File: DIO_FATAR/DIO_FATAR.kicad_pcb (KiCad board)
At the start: 2 copper layers, 92 x 57 mm, 22 parts, among them J1 in, J2 thru, J3 right, J4 left, U1 74HC595, U2 74HC595, U3 74165, U4 74165

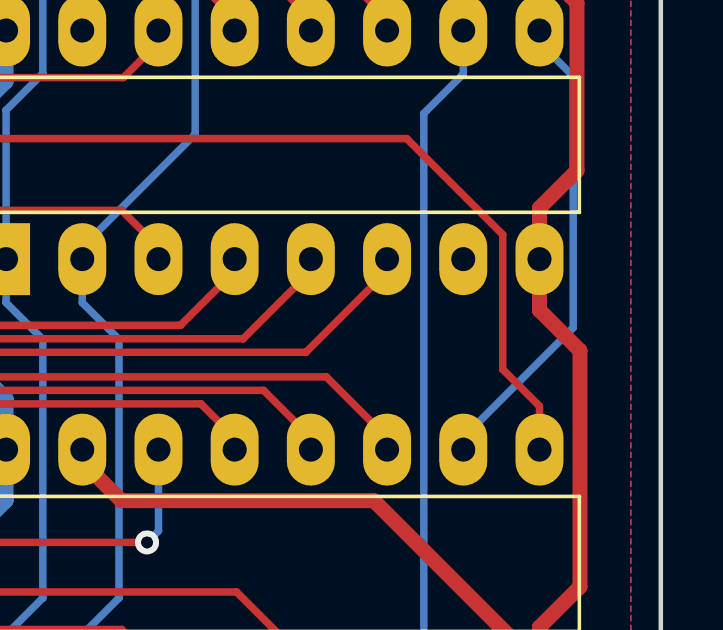
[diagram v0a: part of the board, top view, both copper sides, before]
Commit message: DIO_FATAR: add vias to fill a small empty space
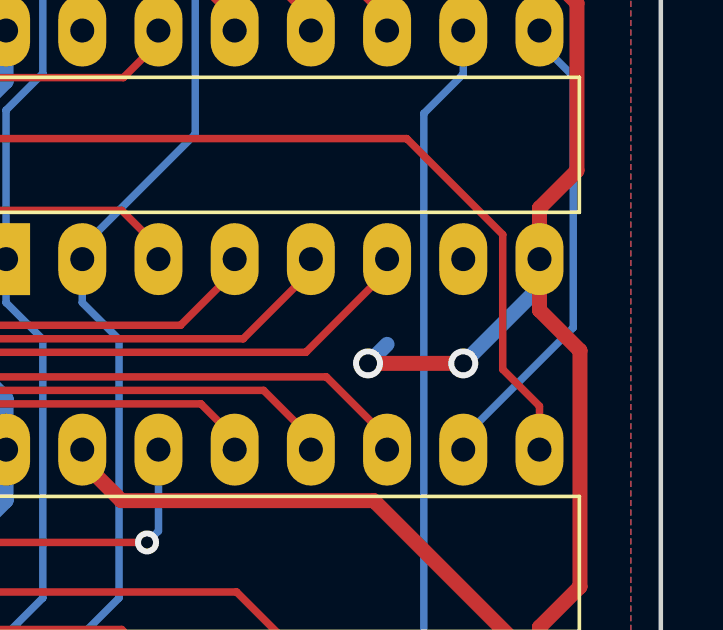
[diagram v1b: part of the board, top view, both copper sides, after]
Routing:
- net GND: track 320.9 -> 329.5 mm, vias 4 -> 6
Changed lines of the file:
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@@
     (thickness 1.6)
     (drawings 4)
-    (tracks 536)
+    (tracks 542)
     (zones 0)
     (modules 22)
@@
   (segment (start 139.458001 56.749999) (end 134.045001 56.749999) (width 0.5) (layer F.Cu) (net 1))
   (segment (start 140.208 56) (end 139.458001 56.749999) (width 0.5) (layer F.Cu) (net 1))
-  (segment (start 130.81 86.06) (end 130.81 85.66) (width 0.25) (layer F.Cu) (net 7))
-  (segment (start 130.81 72.09) (end 130.81 72.49) (width 0.25) (layer B.Cu) (net 7))
-  (segment (start 130.81 71.69) (end 130.81 72.09) (width 0.25) (layer B.Cu) (net 7))
-  (segment (start 140.97 72.49) (end 140.97 72.09) (width 0.25) (layer F.Cu) (net 17))
-  (segment (start 138.43 72.49) (end 138.43 72.09) (width 0.25) (layer F.Cu) (net 19))
-  (segment (start 135.89 72.49) (end 135.89 72.09) (width 0.25) (layer F.Cu) (net 21))
-  (segment (start 133.35 72.09) (end 133.35 71.69) (width 0.25) (layer F.Cu) (net 5))
-  (segment (start 118.745 76.2) (end 114.935 76.2) (width 0.25) (layer F.Cu) (net 21))
-  (segment (start 120.65 74.295) (end 118.745 76.2) (width 0.25) (layer F.Cu) (net 21))
-  (segment (start 135.89 64.47) (end 135.89 64.87) (width 0.25) (layer F.Cu) (net 23))
-  (segment (start 138.43 64.47) (end 138.43 64.07) (width 0.25) (layer F.Cu) (net 25))
-  (segment (start 140.97 64.47) (end 140.97 64.07) (width 0.25) (layer F.Cu) (net 27))
-  (segment (start 140.97 78.44) (end 140.97 78.04) (width 0.25) (layer F.Cu) (net 32))
-  (segment (start 138.43 78.44) (end 138.43 78.04) (width 0.25) (layer F.Cu) (net 33))
   (segment (start 133.35 78.44) (end 133.35 78.84) (width 0.25) (layer B.Cu) (net 2))
   (via (at 134.62 60.452) (size 1) (drill 0.6) (layers F.Cu B.Cu) (net 2))
@@
   (segment (start 130.81 57.865002) (end 133.396998 60.452) (width 0.5) (layer F.Cu) (net 2))
   (segment (start 130.81 54.164998) (end 130.81 57.865002) (width 0.5) (layer F.Cu) (net 2))
+  (segment (start 147.955 72.09) (end 147.955 73.025) (width 0.5) (layer B.Cu) (net 2))
+  (via (at 145.415 75.565) (size 1) (drill 0.6) (layers F.Cu B.Cu) (net 2))
+  (segment (start 147.955 73.025) (end 145.415 75.565) (width 0.5) (layer B.Cu) (net 2))
+  (via (at 142.24 75.565) (size 1) (drill 0.6) (layers F.Cu B.Cu) (net 2))
+  (segment (start 145.415 75.565) (end 142.24 75.565) (width 0.5) (layer F.Cu) (net 2))
+  (segment (start 142.24 75.565) (end 142.875 74.93) (width 0.5) (layer B.Cu) (net 2))
   (via (at 109.22 63.246) (size 0.8) (drill 0.4) (layers F.Cu B.Cu) (net 3))
   (segment (start 107.95 56.515) (end 107.95 61.976) (width 0.25) (layer F.Cu) (net 3))
@@
   (segment (start 105.537 51.562) (end 107.95 53.975) (width 0.25) (layer B.Cu) (net 4))
   (segment (start 91.694 51.562) (end 105.537 51.562) (width 0.25) (layer B.Cu) (net 4))
+  (segment (start 133.35 72.09) (end 133.35 71.69) (width 0.25) (layer F.Cu) (net 5))
   (segment (start 110.49 56.515) (end 110.49 53.975) (width 0.25) (layer B.Cu) (net 5))
   (segment (start 132.715 84.61) (end 132.715 86.06) (width 0.25) (layer B.Cu) (net 5))
@@
   (segment (start 136.48001 67.92499) (end 132.715 71.69) (width 0.25) (layer B.Cu) (net 5))
   (segment (start 110.49 53.975) (end 111.778601 52.686399) (width 0.25) (layer B.Cu) (net 5))
+  (segment (start 130.81 86.06) (end 130.81 85.66) (width 0.25) (layer F.Cu) (net 7))
+  (segment (start 130.81 72.09) (end 130.81 72.49) (width 0.25) (layer B.Cu) (net 7))
+  (segment (start 130.81 71.69) (end 130.81 72.09) (width 0.25) (layer B.Cu) (net 7))
   (segment (start 130.175 84.61) (end 130.175 86.06) (width 0.25) (layer B.Cu) (net 7))
   (segment (start 131.40001 83.38499) (end 130.175 84.61) (width 0.25) (layer B.Cu) (net 7))
@@
   (segment (start 95.866001 68.180001) (end 81.750001 68.180001) (width 0.25) (layer B.Cu) (net 16))
   (segment (start 96.266 68.58) (end 95.866001 68.180001) (width 0.25) (layer B.Cu) (net 16))
+  (segment (start 140.97 72.49) (end 140.97 72.09) (width 0.25) (layer F.Cu) (net 17))
   (segment (start 138.07999 74.74501) (end 140.335 72.49) (width 0.25) (layer F.Cu) (net 17))
   (segment (start 125.27999 74.74501) (end 138.07999 74.74501) (width 0.25) (layer F.Cu) (net 17))
@@
   (segment (start 94.488 76.708) (end 99.06 81.28) (width 0.25) (layer B.Cu) (net 18))
   (segment (start 80.118 76.708) (end 94.488 76.708) (width 0.25) (layer B.Cu) (net 18))
+  (segment (start 138.43 72.49) (end 138.43 72.09) (width 0.25) (layer F.Cu) (net 19))
   (segment (start 137.795 72.49) (end 137.795 72.09) (width 0.25) (layer F.Cu) (net 19))
   (segment (start 135.99 74.295) (end 137.795 72.49) (width 0.25) (layer F.Cu) (net 19))
@@
   (segment (start 96.012 75.692) (end 99.06 78.74) (width 0.25) (layer B.Cu) (net 20))
   (segment (start 81.642 75.692) (end 96.012 75.692) (width 0.25) (layer B.Cu) (net 20))
+  (segment (start 135.89 72.49) (end 135.89 72.09) (width 0.25) (layer F.Cu) (net 21))
+  (segment (start 118.745 76.2) (end 114.935 76.2) (width 0.25) (layer F.Cu) (net 21))
+  (segment (start 120.65 74.295) (end 118.745 76.2) (width 0.25) (layer F.Cu) (net 21))
   (segment (start 135.255 71.69) (end 135.255 72.09) (width 0.25) (layer F.Cu) (net 21))
   (segment (start 134.02999 70.46499) (end 135.255 71.69) (width 0.25) (layer F.Cu) (net 21))
@@
   (segment (start 97.536 74.676) (end 99.06 76.2) (width 0.25) (layer B.Cu) (net 22))
   (segment (start 83.166 74.676) (end 97.536 74.676) (width 0.25) (layer B.Cu) (net 22))
+  (segment (start 135.89 64.47) (end 135.89 64.87) (width 0.25) (layer F.Cu) (net 23))
   (segment (start 119.850001 71.919999) (end 120.65 71.12) (width 0.25) (layer F.Cu) (net 23))
   (segment (start 118.973599 72.796401) (end 119.850001 71.919999) (width 0.25) (layer F.Cu) (net 23))
@@
   (segment (start 82.55 71.52) (end 84.69 73.66) (width 0.25) (layer B.Cu) (net 24))
   (segment (start 82.55 71.12) (end 82.55 71.52) (width 0.25) (layer B.Cu) (net 24))
+  (segment (start 138.43 64.47) (end 138.43 64.07) (width 0.25) (layer F.Cu) (net 25))
   (segment (start 137.795 64.07) (end 137.795 64.47) (width 0.25) (layer F.Cu) (net 25))
   (segment (start 136.66999 62.94499) (end 137.795 64.07) (width 0.25) (layer F.Cu) (net 25))
@@
   (segment (start 85.09 71.52) (end 86.21501 72.64501) (width 0.25) (layer B.Cu) (net 26))
   (segment (start 85.09 71.12) (end 85.09 71.52) (width 0.25) (layer B.Cu) (net 26))
+  (segment (start 140.97 64.47) (end 140.97 64.07) (width 0.25) (layer F.Cu) (net 27))
   (segment (start 118.11 68.58) (end 120.65 66.04) (width 0.25) (layer F.Cu) (net 27))
   (segment (start 114.935 68.58) (end 118.11 68.58) (width 0.25) (layer F.Cu) (net 27))
@@
   (segment (start 102.235 66.675) (end 101.6 66.04) (width 0.25) (layer B.Cu) (net 31))
   (segment (start 106.68 66.675) (end 102.235 66.675) (width 0.25) (layer B.Cu) (net 31))
+  (segment (start 140.97 78.44) (end 140.97 78.04) (width 0.25) (layer F.Cu) (net 32))
   (segment (start 102.235 69.215) (end 101.6 68.58) (width 0.25) (layer B.Cu) (net 32))
   (segment (start 106.68 69.215) (end 102.235 69.215) (width 0.25) (layer B.Cu) (net 32))
@@
   (segment (start 122.555 72.39) (end 122.555 71.359998) (width 0.25) (layer B.Cu) (net 32))
   (segment (start 127.635 77.47) (end 122.555 72.39) (width 0.25) (layer B.Cu) (net 32))
+  (segment (start 138.43 78.44) (end 138.43 78.04) (width 0.25) (layer F.Cu) (net 33))
   (segment (start 102.235 71.755) (end 101.6 71.12) (width 0.25) (layer B.Cu) (net 33))
   (segment (start 106.68 71.755) (end 102.235 71.755) (width 0.25) (layer B.Cu) (net 33))
@@
   (segment (start 125.73 85.725) (end 124.46 85.725) (width 0.25) (layer F.Cu) (net 38))
   (segment (start 128.14001 88.13501) (end 125.73 85.725) (width 0.25) (layer F.Cu) (net 38))
-  (segment (start 149.08001 74.37499) (end 145.415 78.04) (width 0.25) (layer B.Cu) (net 52))
-  (segment (start 145.415 78.04) (end 145.415 78.44) (width 0.25) (layer B.Cu) (net 52))
-  (segment (start 149.08001 65.99501) (end 149.08001 74.37499) (width 0.25) (layer B.Cu) (net 52))
-  (segment (start 147.955 64.87) (end 149.08001 65.99501) (width 0.25) (layer B.Cu) (net 52))
-  (segment (start 147.955 64.47) (end 147.955 64.87) (width 0.25) (layer B.Cu) (net 52))
   (segment (start 83.82 74.53) (end 83.82 67.31) (width 0.25) (layer F.Cu) (net 45))
   (segment (start 80.01 78.74) (end 80.01 78.34) (width 0.25) (layer F.Cu) (net 45))
@@
   (segment (start 92.71 63.9) (end 89.916 66.694) (width 0.25) (layer F.Cu) (net 45))
   (segment (start 89.916 67.31) (end 83.82 67.31) (width 0.25) (layer B.Cu) (net 45))
+  (segment (start 149.08001 74.37499) (end 145.415 78.04) (width 0.25) (layer B.Cu) (net 52))
+  (segment (start 145.415 78.04) (end 145.415 78.44) (width 0.25) (layer B.Cu) (net 52))
+  (segment (start 149.08001 65.99501) (end 149.08001 74.37499) (width 0.25) (layer B.Cu) (net 52))
+  (segment (start 147.955 64.87) (end 149.08001 65.99501) (width 0.25) (layer B.Cu) (net 52))
+  (segment (start 147.955 64.47) (end 147.955 64.87) (width 0.25) (layer B.Cu) (net 52))
   (segment (start 147.828 64.343) (end 147.955 64.47) (width 0.25) (layer B.Cu) (net 52))
   (segment (start 147.955 56.127) (end 147.828 56) (width 0.25) (layer B.Cu) (net 52))
